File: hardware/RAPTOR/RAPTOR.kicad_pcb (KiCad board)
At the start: 2 copper layers, 101.6 x 55.9 mm, 45 parts, among them J1 SOLC_CONN, J10 EXT_LED3, J11 SRVOL_CONN, J12 SRVOR_CONN, J13 HOTWIRE_CONN, J14 RBF_CONN, J15 EEPROM_BTN_CONN, J16 SOLC_SW_CONN, J17 SOLP_SW_CONN, J2 SOLP_CONN, J3 CONN_01X01, J3 JST_2MM_MALE, J4 CONN_LED_FIX, J5 CONN_SOLP_LED, J6 CONN_SOLC_LED, J7 EXT_LED0, J8 EXT_LED1, J9 EXT_LED2, P1 Power, P2 Analog, P3 Digital, P4 Digital, P5 Digital, P7 CONN_01X01, P8 CONN_01X01, Q1 MOSFET-NCH-STQ2NK60ZR-AP, Q2 MOSFET-NCH-STQ2NK60ZR-AP, Q3 MOSFET-NCH-STQ2NK60ZR-AP, Q4 MOSFET-NCH-STQ2NK60ZR-AP, Q5 MOSFET-NCH-STQ2NK60ZR-AP, U1 BMP280 Breakout, U2 BNO055 Breakout, U2 OpenLog, U3 OpenLog, U4 AdafruitGPS, U5 U3V12F12, U6 D24V550F5

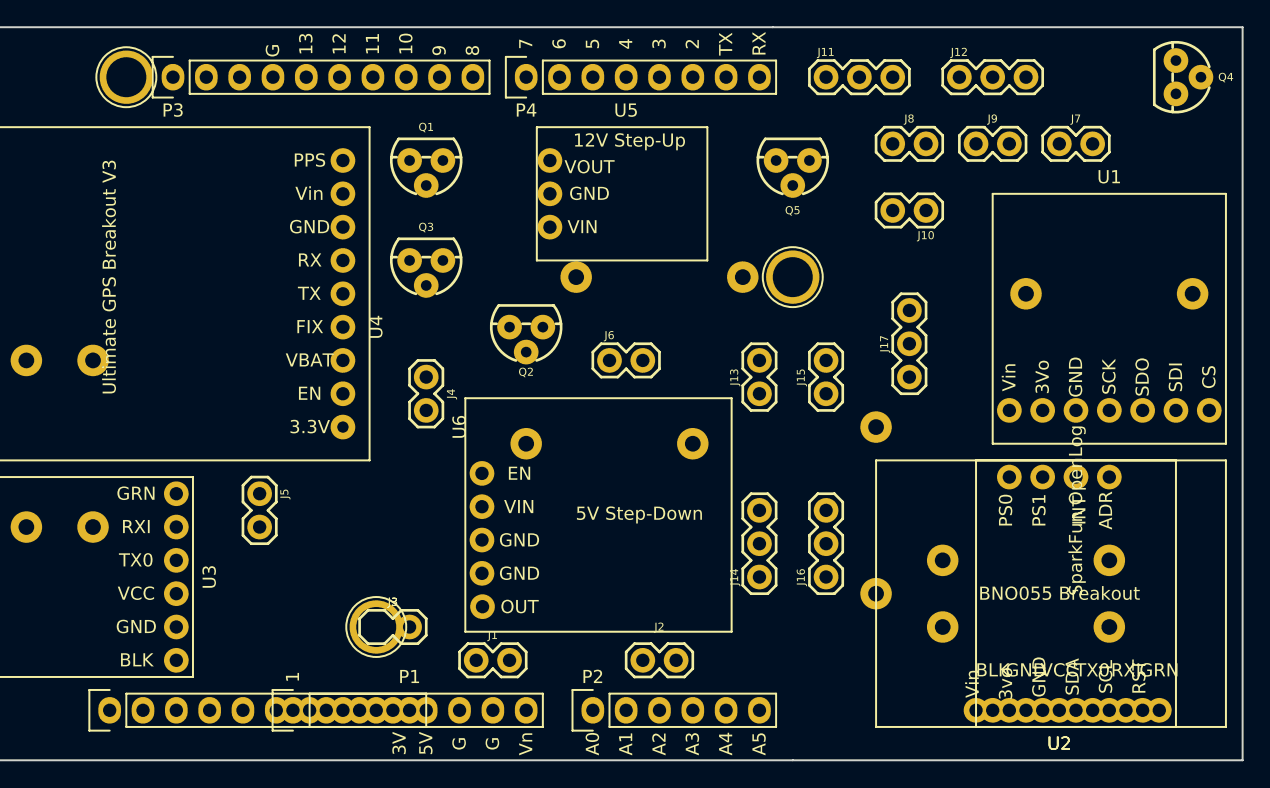
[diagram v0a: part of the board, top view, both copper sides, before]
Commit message: add mosfet silkscreen, update pcb
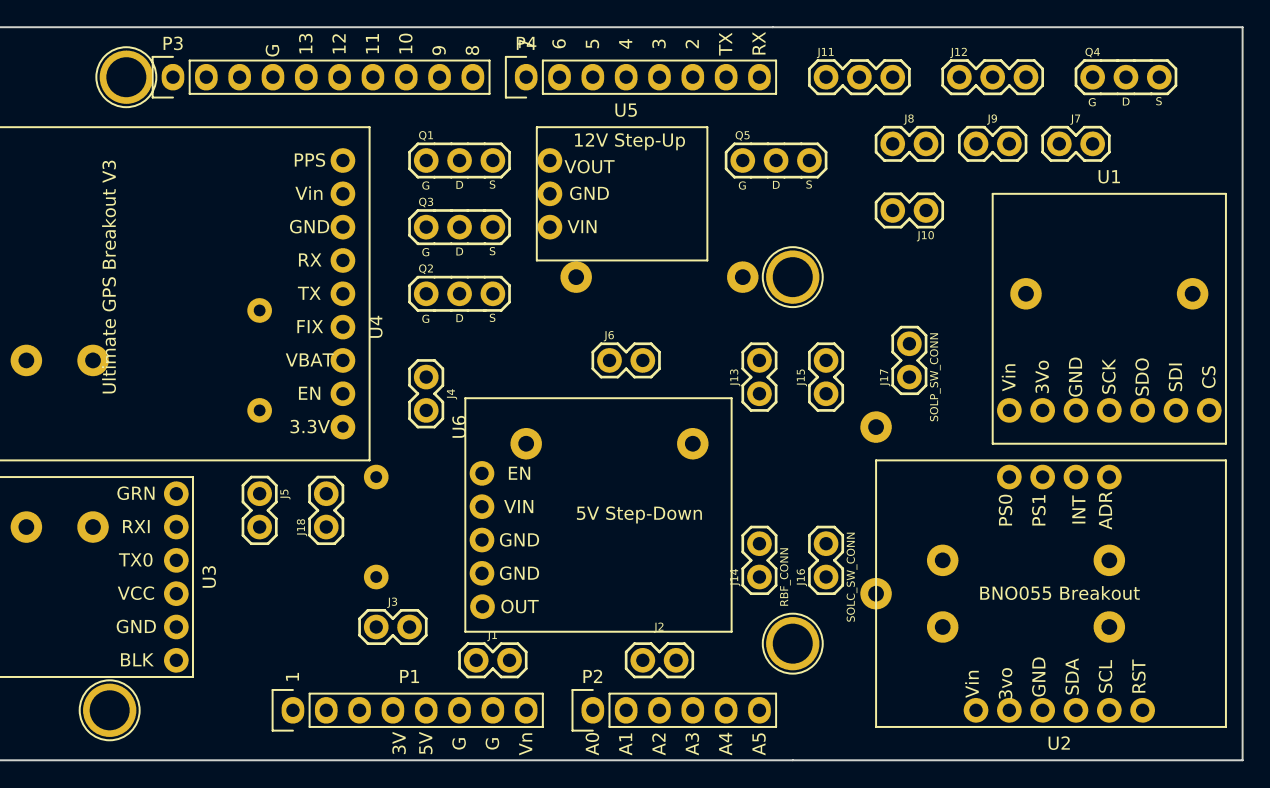
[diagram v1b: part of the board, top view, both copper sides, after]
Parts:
- removed the J3 at (145.3, 117.5) (x2)
- removed the U2 at (197.4, 123.8) (x2)
- added D8: >VALUE, Silicon-Custom:DIODE-1N4148, B.Cu at (145.3, 109.9)
- added D9: >VALUE, Silicon-Custom:DIODE-1N4148, B.Cu at (136.4, 97.2)
- added J18: CONN_BUZZER, Connectors:1X02, F.Cu at (141.5, 109.9)
- added J3: JST_2MM_MALE, RAPTOR_footprints:2_Pin_Connector, F.Cu at (145.3, 117.5)
- added P6: CONN_01X01, Socket_Arduino_Uno:Arduino_1pin, F.Cu at (177.0, 118.7)
- added U2: BNO055 Breakout, RAPTOR_footprints:BNO055, F.Cu at (197.4, 123.8)
- J14, J16, J17: footprint Connectors:1X03 -> Connectors:1X02
- P5: value Digital -> CONN_01X01
- Q1, Q2, Q3, Q4, Q5: footprint Silicon-Standard:TO-92 -> RAPTOR_footprints:MOSFET
- moved Q2 8.03 mm to (149.1, 92.1), turned to 0 degrees
- moved Q4 6.35 mm to (199.9, 75.6), turned to 0 degrees
- moved Q5 3.81 mm to (173.2, 81.9), turned to 0 degrees
- moved Q3 2.54 mm to (149.1, 87.0), turned to 0 degrees
- turned Q1 to 0 degrees

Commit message: merge
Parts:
- D8, D9: value >VALUE -> DIODE-1N4148
- J1, J10, J13, J14, J15, J16, J17, J18, J2, J4, J5, J6, J7, J8, J9: footprint Connectors:1X02 -> RAPTOR_footprints:Molex-2pin
- J11, J12: footprint Connectors:1X03 -> RAPTOR_footprints:Molex-MOTOR
- U1, U2: moved to B.Cu
- moved R6 95.6 mm to (252.0, 55.2)
- moved R3 94.8 mm to (263.4, 61.6)
- moved Q4 77.8 mm to (135.1, 118.7)
- moved R4 72.9 mm to (243.1, 60.3)
- moved R1 67.6 mm to (220.2, 57.8)
- moved D9 57.7 mm to (91.9, 134.0)
- moved D8 54.0 mm to (97.0, 134.0)
- moved R8 51.6 mm to (220.2, 71.8)
- moved U5 48.6 mm to (197.4, 108.6)
- moved Q5 47.0 mm to (144.0, 118.7)
- moved J7 45.5 mm to (155.4, 98.4)
- moved U6 39.0 mm to (191.0, 89.5)
- moved R7 37.8 mm to (220.2, 64.1)
- moved R2 35.2 mm to (91.9, 112.4)
- moved Q3 31.2 mm to (135.1, 114.9)
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
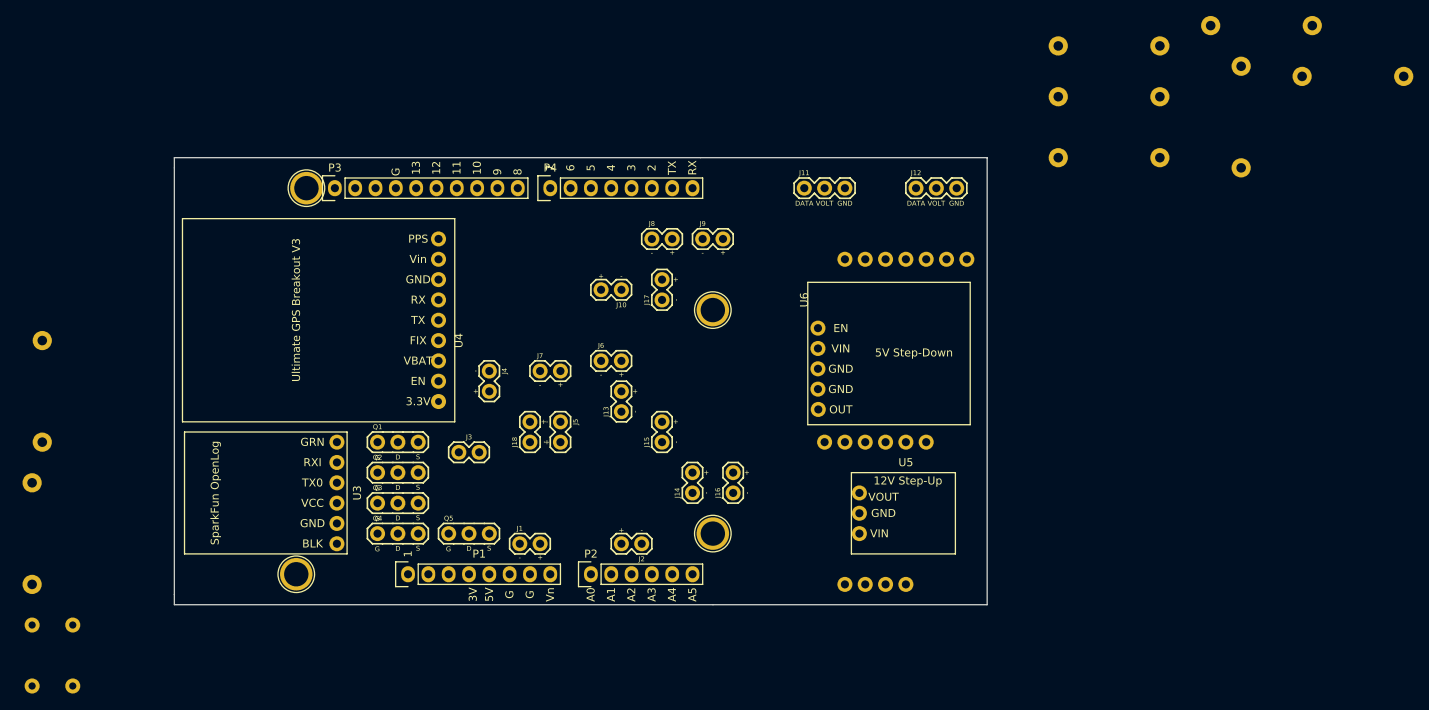
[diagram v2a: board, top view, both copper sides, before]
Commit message: Organized PCB Layout
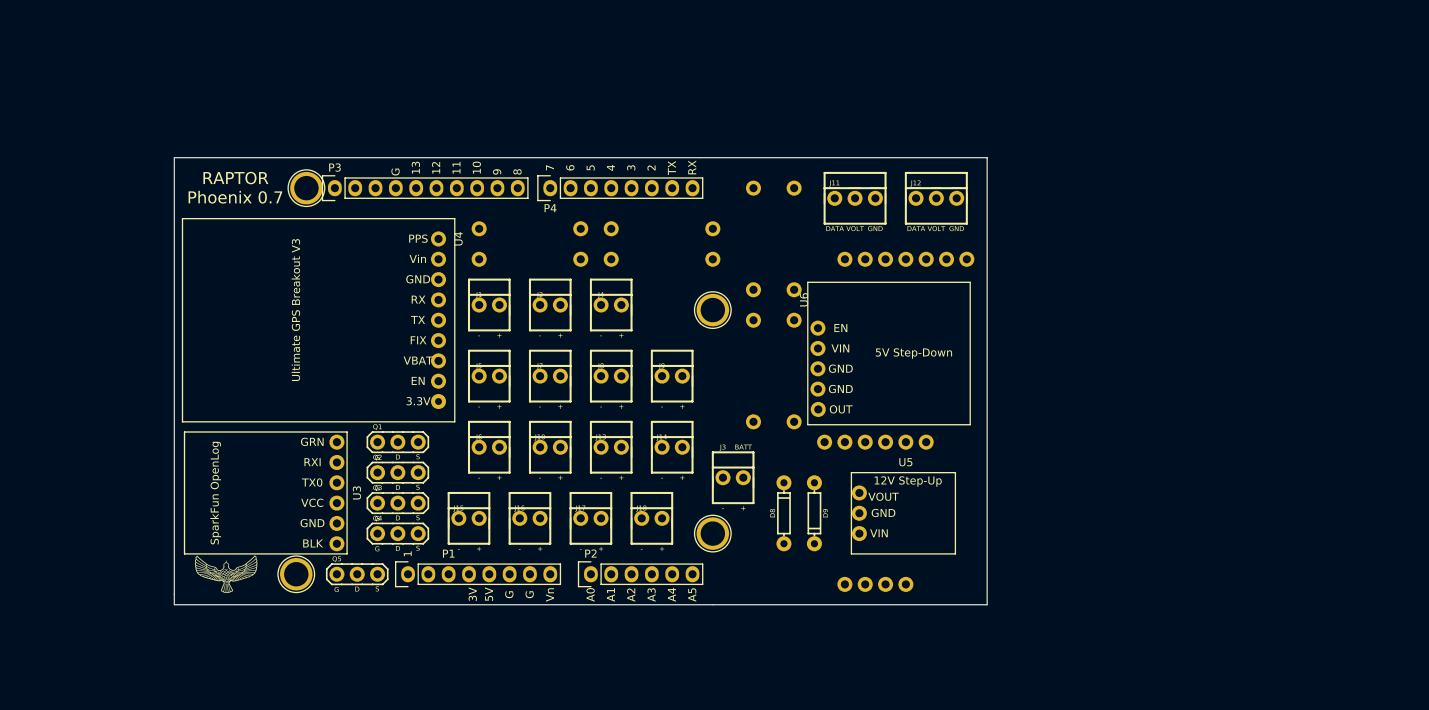
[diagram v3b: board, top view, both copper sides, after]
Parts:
- added G***: LOGO, RAPTOR_footprints:BirdLogo, F.Cu at (116.1, 123.8)
- D8, D9: moved to F.Cu
- J3: footprint RAPTOR_footprints:2_Pin_Connector -> RAPTOR_footprints:Molex-BATT
- R1, R2, R3, R4, R5, R6, R7, R8: footprint Resistor_THT:R_Axial_DIN0411_L9.9mm_D3.6mm_P12.70mm_Horizontal -> RAPTOR_footprints:Resistor
- moved D9 99.4 mm to (189.7, 116.2)
- moved D8 90.7 mm to (185.9, 116.2), turned to 90 degrees
- moved R5 89.1 mm to (182.1, 88.3), turned to 90 degrees
- moved R3 88.4 mm to (177.0, 80.6)
- moved R4 82.4 mm to (164.3, 84.5), turned to 0 degrees
- moved R1 75.9 mm to (147.8, 80.6)
- moved R6 67.9 mm to (187.2, 75.6), turned to 270 degrees
- moved R2 62.5 mm to (147.8, 84.5), turned to 0 degrees
- moved R7 55.7 mm to (182.1, 104.8), turned to 90 degrees
- moved R8 46.7 mm to (187.2, 104.8), turned to 90 degrees
- moved J3 33.2 mm to (178.3, 112.4)
- moved J2 31.9 mm to (155.4, 90.8), turned to 0 degrees
- moved J17 29.7 mm to (160.5, 117.5), turned to 0 degrees
- moved J1 29.6 mm to (147.8, 90.8)
- moved J15 27.4 mm to (145.3, 117.5), turned to 0 degrees
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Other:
- board text added: "RAPTOR Phoenix 0.7"

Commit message: Adjust 1 board
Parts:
- moved U6 0.63 mm to (191.6, 89.5)
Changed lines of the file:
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@@
   )
   (module RAPTOR_footprints:D24v50f5_Reg (layer F.Cu)
-    (at 191.008 89.535 270)
+    (at 191.643 89.535 270)
     (fp_text reference U6 (at 0 2.54 270) (layer F.SilkS)
       (effects (font (size 1 1) (thickness 0.15)))

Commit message: Start the Routing
Lets Go dude
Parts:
- moved J15 25.4 mm to (170.7, 117.5)
- moved J18 22.9 mm to (145.3, 117.5)
- turned D8 to 270 degrees
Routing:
- net +5V: track 0.00 -> 122.6 mm
- net /HOTWIRE: track 0.00 -> 97.0 mm
- net /SD_TX: track 0.00 -> 95.7 mm
- net /SD_RX: track 0.00 -> 87.8 mm
- net +7.5V: track 0.00 -> 79.9 mm
- net /I2C_SDA: track 0.00 -> 63.0 mm
- net /I2C_SCL: track 0.00 -> 60.8 mm
- net /SOLC_DTA: track 0.00 -> 52.3 mm
- net /LEDS_DTA: track 0.00 -> 49.6 mm
- net +3V3: track 0.00 -> 46.9 mm
- net /SRVO_R: track 0.00 -> 46.1 mm
- net /BZZ_DTA: track 0.00 -> 44.5 mm
- net Net-(J10-Pad1): track 0.00 -> 41.7 mm
- net /GPS_TX: track 0.00 -> 40.2 mm
- net /SOLP_DTA: track 0.00 -> 39.7 mm
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
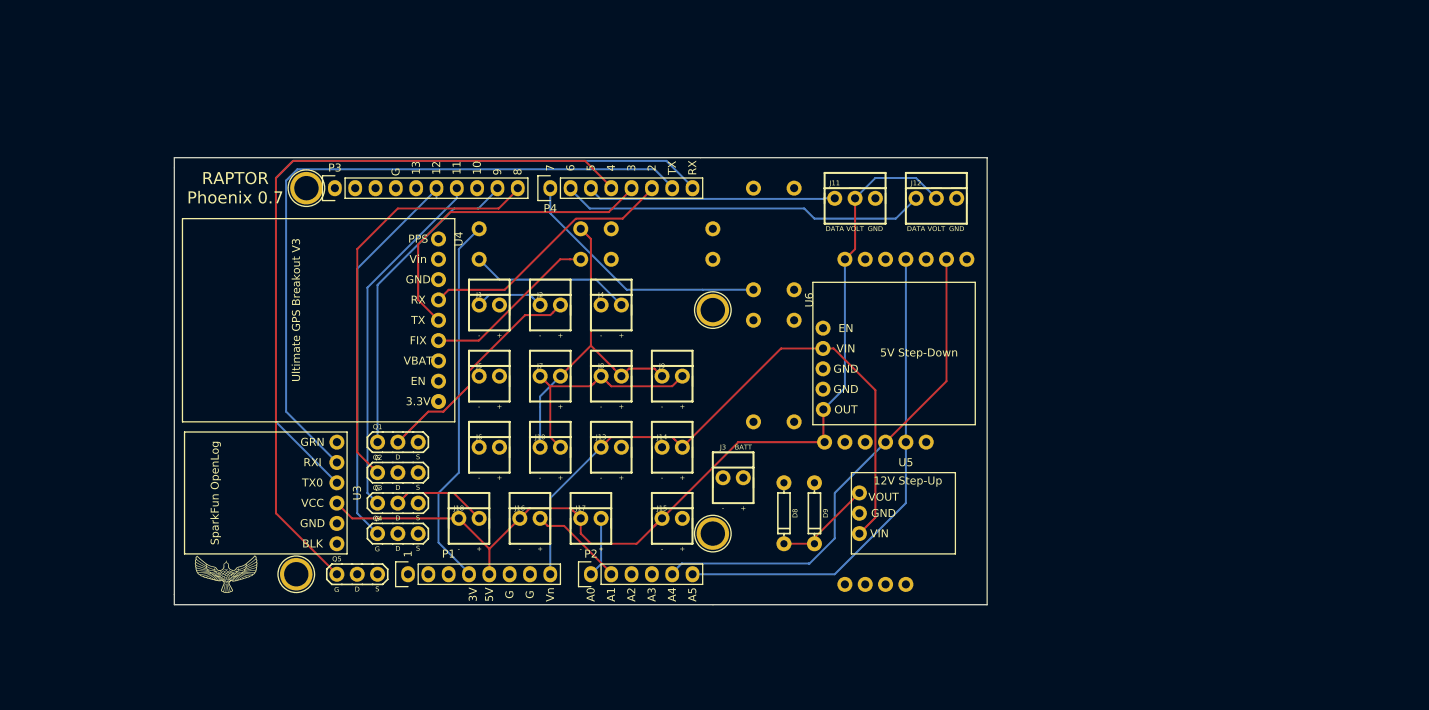
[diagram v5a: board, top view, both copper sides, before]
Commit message: All Routed w/o RXTX button
All the connections are made except for the rx and tx button
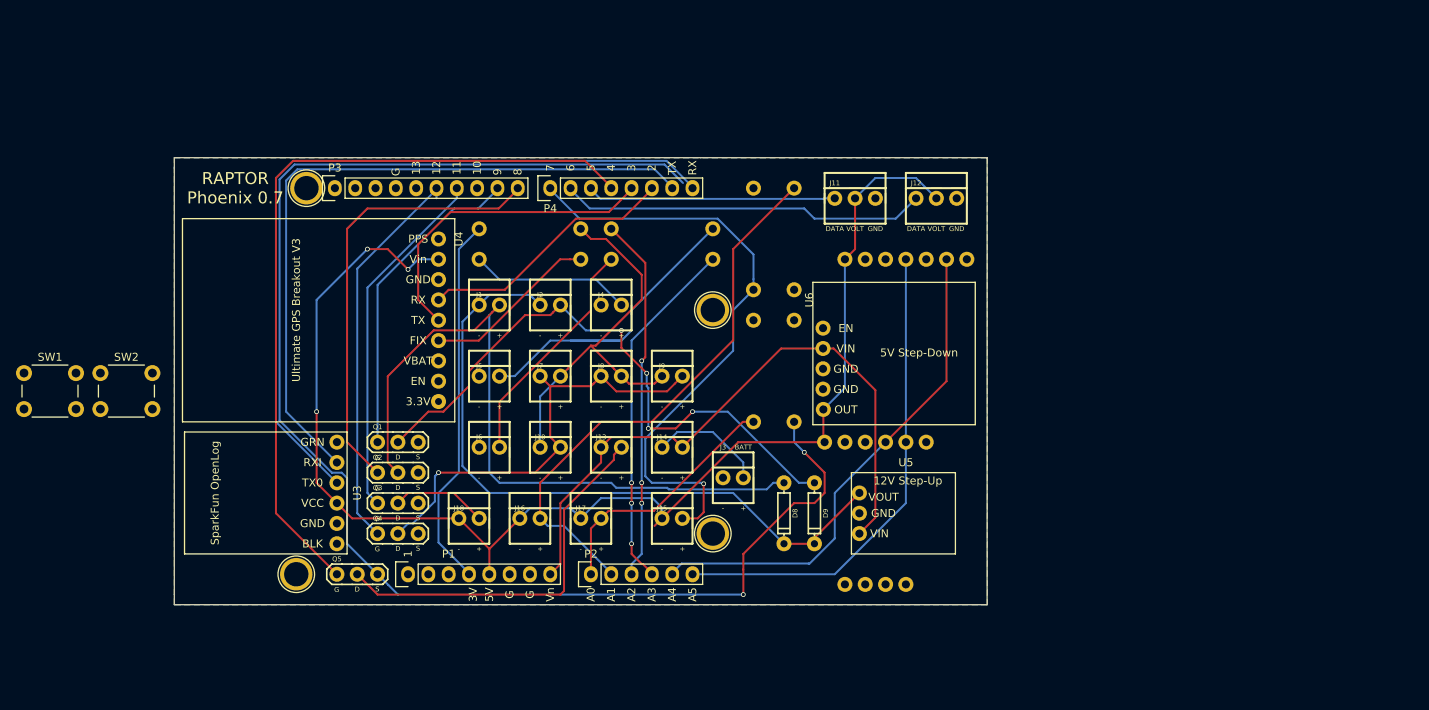
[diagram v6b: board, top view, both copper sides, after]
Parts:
- removed G***: LOGO, RAPTOR_footprints:BirdLogo
- added SW1: SW_Push_Open, Button_Switch_THT:SW_PUSH_6mm, F.Cu at (90.9, 98.7)
- added SW2: SW_Push_Open, Button_Switch_THT:SW_PUSH_6mm, F.Cu at (100.5, 98.7)
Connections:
- U3 pad 2: /SD_RX -> Net-(SW1-Pad1)
- U3 pad 3: /SD_TX -> Net-(SW2-Pad1)
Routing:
- net Net-(Q5-Pad2): track 0.00 -> 182.9 mm, vias 0 -> 2
- net Net-(D8-PadA): track 0.00 -> 89.7 mm
- net +12V: track 21.2 -> 86.4 mm
- net /SOLC_SW: track 11.9 -> 70.2 mm
- net Net-(J13-Pad2): track 0.00 -> 48.0 mm
- net Net-(D9-PadA): track 28.5 -> 76.4 mm, vias 0 -> 4
- net /LEDP_DTA: track 0.00 -> 45.7 mm, vias 0 -> 3
- net +5V: track 122.6 -> 167.6 mm, vias 0 -> 3
- net /LEDC_DTA: track 0.00 -> 44.7 mm, vias 0 -> 3
- net /EEPROM_BTN: track 32.7 -> 76.5 mm, vias 0 -> 1
- net Net-(J5-Pad2): track 0.00 -> 42.1 mm
- net Net-(J6-Pad2): track 0.00 -> 29.3 mm
- net Net-(J10-Pad2): track 28.0 -> 55.2 mm, vias 0 -> 1
- net /SOLP_SW: track 7.51 -> 31.6 mm
- net Net-(J14-Pad1): track 0.00 -> 14.4 mm
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- added copper zone on B.Cu, net GND
- added copper zone on F.Cu, net GND
